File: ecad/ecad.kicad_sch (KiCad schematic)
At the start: 48 parts, among them J1 JTAG, J2 USB_C, J3 Display, Q2 SS8050, SW10 RotaryEncoder_Switch, SW11 RotaryEncoder_Switch, SW15 RESET, SW24 Kailh choc v2, SW25 Kailh choc v2, U1 AP2112K-3.3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

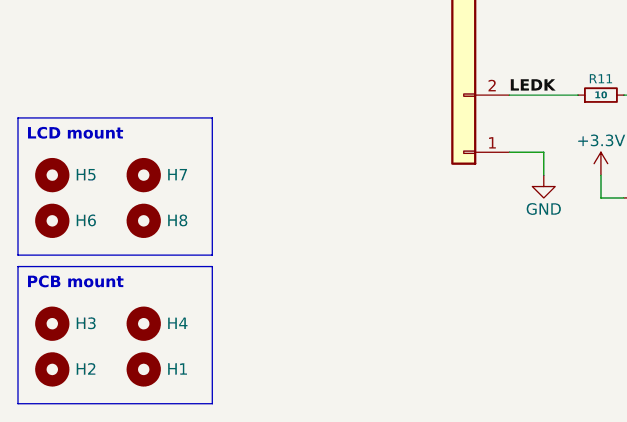
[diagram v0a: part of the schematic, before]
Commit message: feat(ecad): ws2812b placement and routing
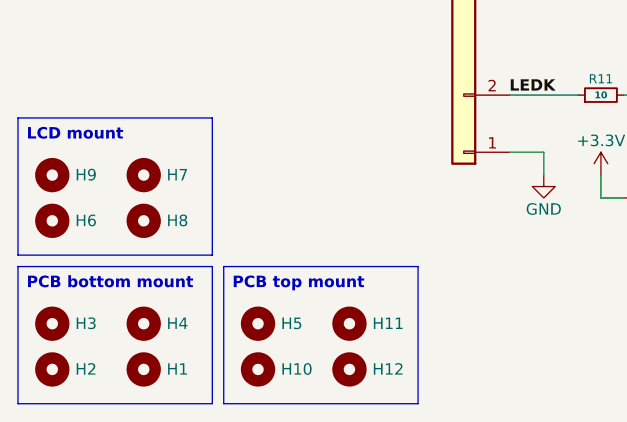
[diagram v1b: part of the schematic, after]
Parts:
- added H10, H11, H12, H9: MountingHole, MountingHole:MountingHole_2.2mm_M2_DIN965, symbol Mechanical:MountingHole
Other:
- moved on the sheet: H5

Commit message: fix(ecad): change screw holes size
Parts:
- H1, H10, H11, H12, H2, H3, H4, H5: footprint MountingHole:MountingHole_2.2mm_M2_DIN965 -> MountingHole:MountingHole_3.2mm_M3_DIN965
- J2: footprint Connector_USB:USB_C_Receptacle_JAE_DX07S016JA1R1500 -> Connector_USB:USB_C_Receptacle_Amphenol_12401948E412A
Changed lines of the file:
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@@
 			)
 		)
-		(property "Footprint" "Connector_USB:USB_C_Receptacle_JAE_DX07S016JA1R1500"
+		(property "Footprint" "Connector_USB:USB_C_Receptacle_Amphenol_12401948E412A"
 			(at 254 40.64 0)
 			(effects
@@
 			)
 		)
-		(property "Footprint" "MountingHole:MountingHole_2.2mm_M2_DIN965"
+		(property "Footprint" "MountingHole:MountingHole_3.2mm_M3_DIN965"
 			(at 27.94 191.77 0)
 			(effects
@@
 			)
 		)
-		(property "Footprint" "MountingHole:MountingHole_2.2mm_M2_DIN965"
+		(property "Footprint" "MountingHole:MountingHole_3.2mm_M3_DIN965"
 			(at 50.8 191.77 0)
 			(effects
@@
 			)
 		)
-		(property "Footprint" "MountingHole:MountingHole_2.2mm_M2_DIN965"
+		(property "Footprint" "MountingHole:MountingHole_3.2mm_M3_DIN965"
 			(at 40.64 186.69 0)
 			(effects
@@
 			)
 		)
-		(property "Footprint" "MountingHole:MountingHole_2.2mm_M2_DIN965"
+		(property "Footprint" "MountingHole:MountingHole_3.2mm_M3_DIN965"
 			(at 50.8 186.69 0)
 			(effects
@@
 			)
 		)
-		(property "Footprint" "MountingHole:MountingHole_2.2mm_M2_DIN965"
+		(property "Footprint" "MountingHole:MountingHole_3.2mm_M3_DIN965"
 			(at 40.64 191.77 0)
 			(effects
@@
 			)
 		)
-		(property "Footprint" "MountingHole:MountingHole_2.2mm_M2_DIN965"
+		(property "Footprint" "MountingHole:MountingHole_3.2mm_M3_DIN965"
 			(at 17.78 191.77 0)
 			(effects
@@
 			)
 		)
-		(property "Footprint" "MountingHole:MountingHole_2.2mm_M2_DIN965"
+		(property "Footprint" "MountingHole:MountingHole_3.2mm_M3_DIN965"
 			(at 17.78 186.69 0)
 			(effects
@@
 			)
 		)
-		(property "Footprint" "MountingHole:MountingHole_2.2mm_M2_DIN965"
+		(property "Footprint" "MountingHole:MountingHole_3.2mm_M3_DIN965"
 			(at 27.94 186.69 0)
 			(effects

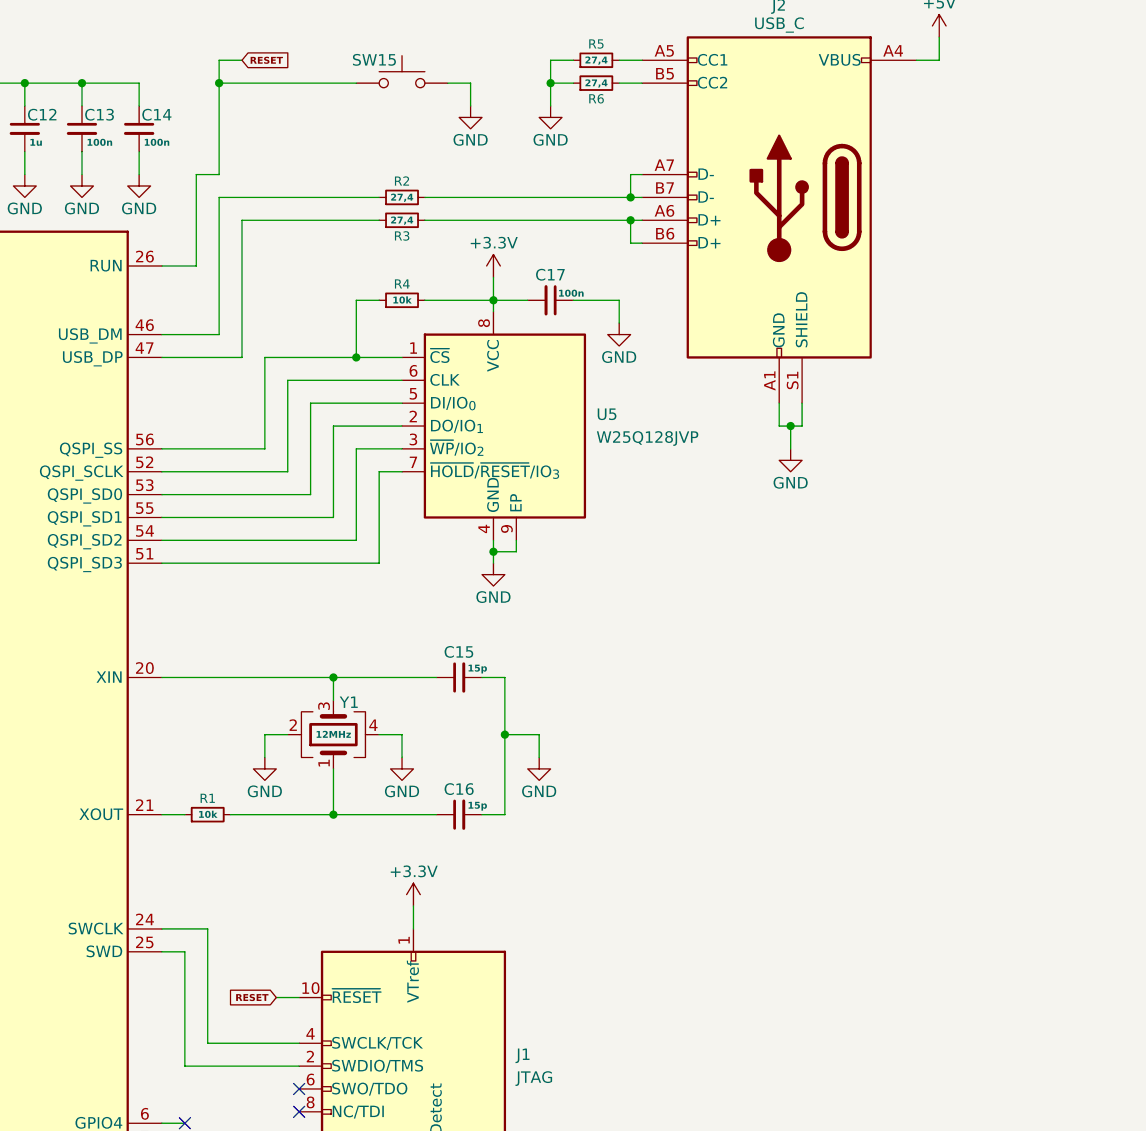
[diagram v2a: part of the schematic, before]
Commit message: fix(ecad): change board dimensions
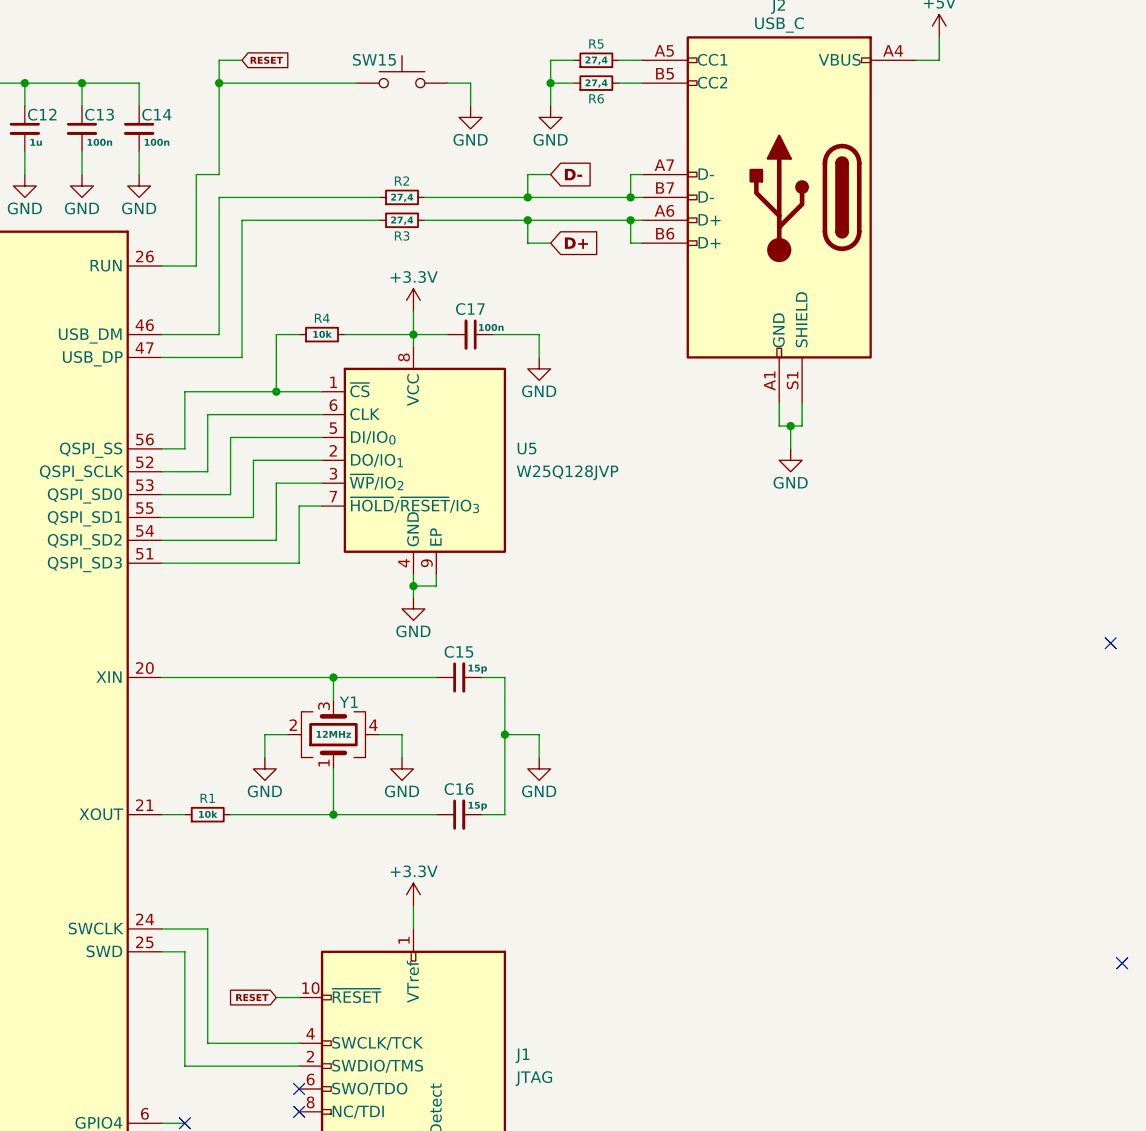
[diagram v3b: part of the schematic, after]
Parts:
- H1, H2, H3, H4: footprint MountingHole:MountingHole_3.2mm_M3_DIN965 -> sinhoo-smtso3030ctj:smtso3030ctj
- Y1: footprint Crystal:Crystal_SMD_Abracon_ABM8AIG-4Pin_3.2x2.5mm -> Crystal:Crystal_SMD_Abracon_ABM8G-4Pin_3.2x2.5mm
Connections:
- net D+: now reaches J2.A6 (D+), J2.B6 (D+), R3.2
- net D-: now reaches J2.A7 (D-), J2.B7 (D-), R2.2
- no-connect marks 9 -> 11
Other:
- moved on the sheet: C17, R4, U5

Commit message: feat(ecad): add pcb nuts on pcb
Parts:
- SW24, SW25: value Kailh choc v2 -> ~
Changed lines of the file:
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@@
 			)
 		)
-		(property "Value" "Kailh choc v2"
+		(property "Value" "~"
 			(at 192.786 172.72 0)
 			(effects
@@
 			)
 		)
-		(property "Value" "Kailh choc v2"
+		(property "Value" "~"
 			(at 192.786 166.37 0)
 			(effects

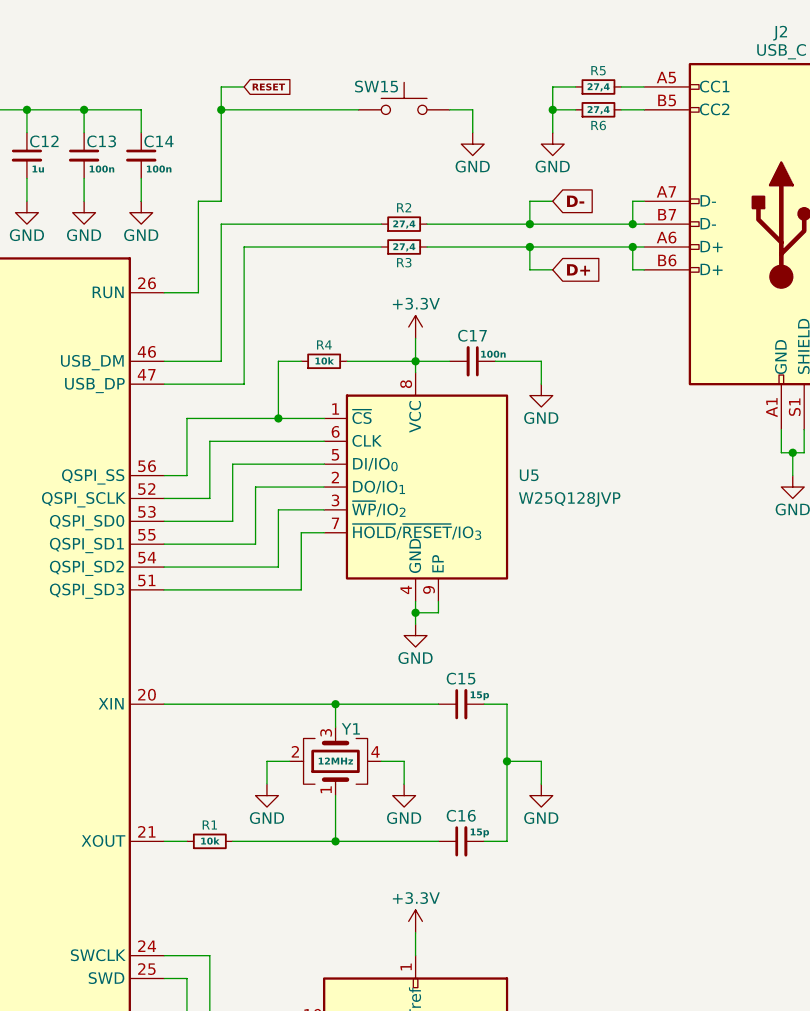
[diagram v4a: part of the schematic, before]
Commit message: feat(ecad): update schematics and README with hardware documentation
- Update KiCad schematics (main, LEDs, switches sub-sheets)
- Update PCB layout
- Rewrite README with full hardware specs, GPIO map, architecture
  overview, key config format and commit convention
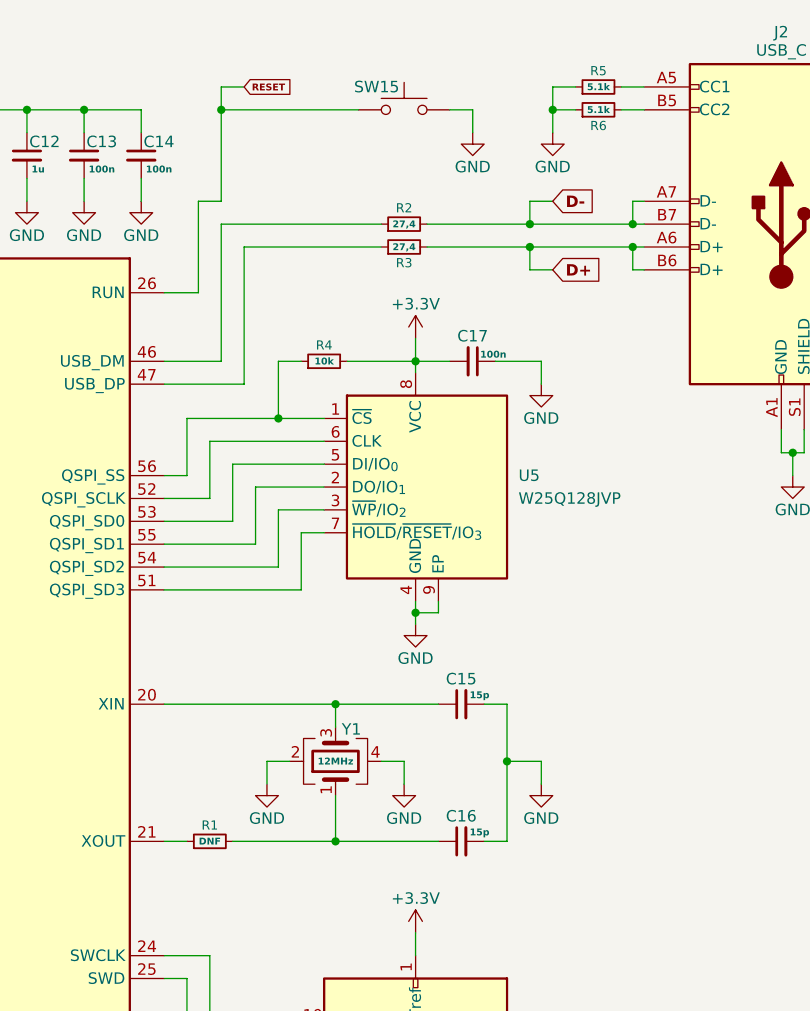
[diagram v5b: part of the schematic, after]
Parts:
- R1: value 10k -> DNF
- R5, R6: value 27,4 -> 5.1k
- SW24, SW25: value ~ -> (none)

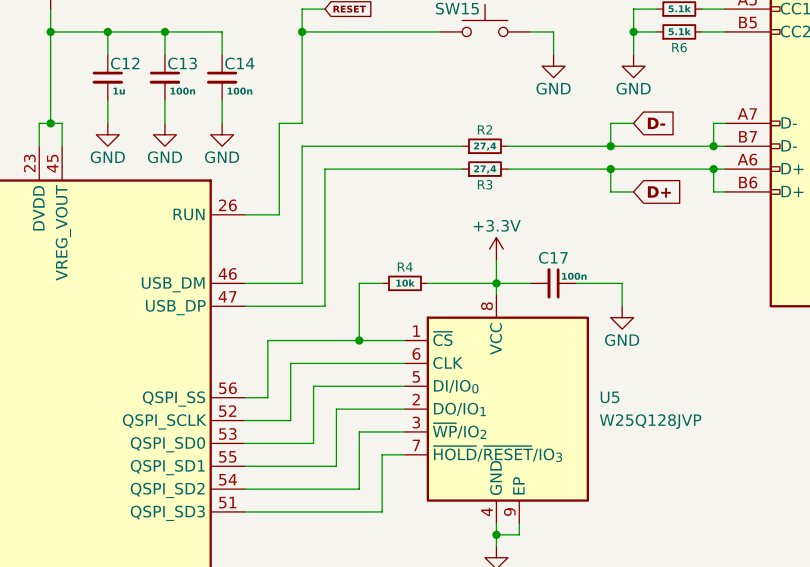
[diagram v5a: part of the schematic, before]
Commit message: fix(ecad): change sur resistor and capacitor value to ajust
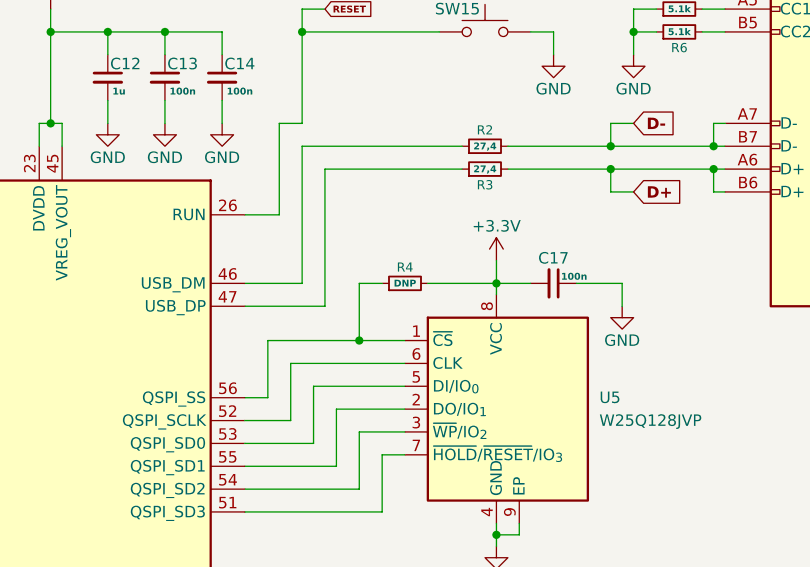
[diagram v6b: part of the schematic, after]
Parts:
- R4: value 10k -> DNP
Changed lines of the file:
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@@
 			)
 		)
-		(property "Value" "10k"
+		(property "Value" "DNP"
 			(at 207.01 55.88 90)
 			(show_name no)

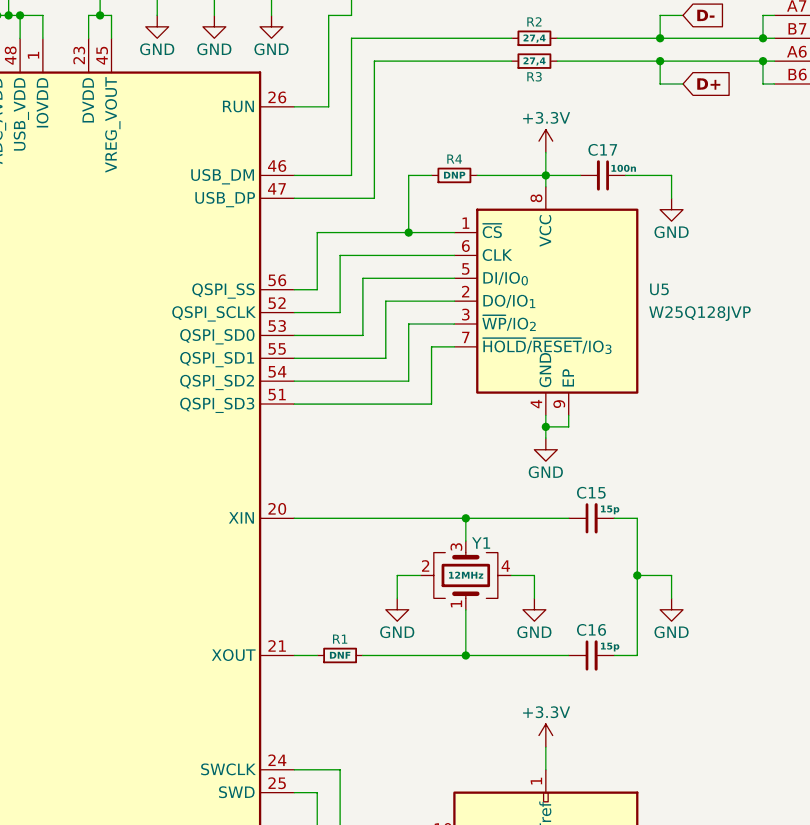
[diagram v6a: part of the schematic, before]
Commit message: fix(ecad): mark R4 as DNP and update zone fill defaults
R4 set to do-not-place with value corrected to 0.
Zone fill parameters expanded in project file (thermal relief, hatch, clearance).
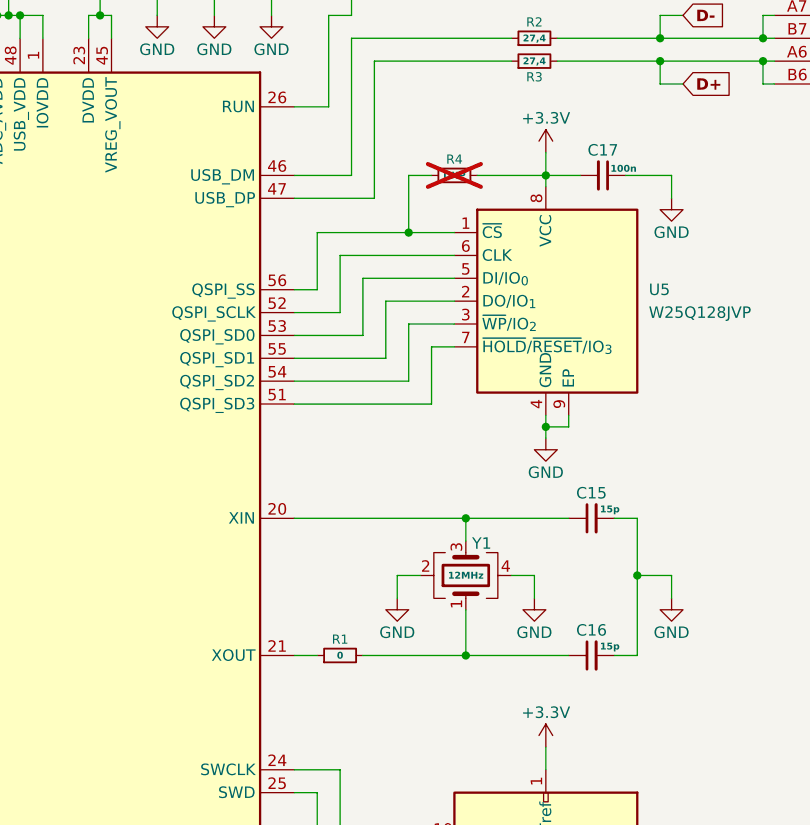
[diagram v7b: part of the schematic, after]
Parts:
- R1: value DNF -> 0
- R4: now not fitted
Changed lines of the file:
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@@
 		(on_board yes)
 		(in_pos_files yes)
-		(dnp no)
+		(dnp yes)
 		(property "Reference" "R4"
 			(at 207.01 54.102 90)
@@
 			)
 		)
-		(property "Value" "DNF"
+		(property "Value" "0"
 			(at 194.31 109.22 90)
 			(show_name no)
